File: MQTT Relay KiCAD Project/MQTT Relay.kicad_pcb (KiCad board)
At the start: 2 copper layers, 63.5 x 53.3 mm, 19 parts, among them J1 Power, J2 Temp 0, J3 Input 0, J4 Input 1, J5 Relay 0, J6 Relay 1, SW1 SW_Push, SW2 SW_Push, SW3 SW_Push, U1 SSD1306_128x32

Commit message: Added DFPlayer support
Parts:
- added J7: Line Out, TerminalBlock_Phoenix:TerminalBlock_Phoenix_MPT-0,5-3-2.54_1x03_P2.54mm_Horizontal, F.Cu at (147.3, 78.1)
- added R5: 1K, Resistor_THT:R_Axial_DIN0207_L6.3mm_D2.5mm_P10.16mm_Horizontal, F.Cu at (128.9, 71.8)
- added U2: DFPlayer_Module, Module:Module_DIP16_17.8mm, F.Cu at (139.7, 60.3)
- moved J1 56.8 mm to (77.5, 77.5), turned to -90 degrees
- moved J2 45.4 mm to (147.3, 87.6)
- moved J6 28.5 mm to (148.6, 40.6), turned to 180 degrees
- moved J5 14.9 mm to (138.4, 40.6), turned to 180 degrees
- moved J3 14.2 mm to (135.9, 86.4), turned to 0 degrees
- moved J4 8.13 mm to (128.3, 86.4), turned to 0 degrees
- moved e 7.62 mm to (125.7, 78.7)
- moved REF** 1.27 mm to (127.0, 40.6)
- moved SW2 1.24 mm to (113.0, 39.4)
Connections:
- net /~CFG renamed /~{CFG}
- A1 pad 15: Net-(A1-Pad15) -> unconnected-(A1-Pad15)
- A1 pad 16: Net-(A1-Pad16) -> unconnected-(A1-Pad16)
- A1 pad 20: Net-(A1-Pad20) -> unconnected-(A1-Pad20)
- A1 pad 21: Net-(A1-Pad21) -> unconnected-(A1-Pad21)
- A1 pad 22: Net-(A1-Pad22) -> unconnected-(A1-Pad22)
- A1 pad 23: Net-(A1-Pad23) -> unconnected-(A1-Pad23)
- A1 pad 24: Net-(A1-Pad24) -> unconnected-(A1-Pad24)
- A1 pad 27: Net-(A1-Pad27) -> unconnected-(A1-Pad27)
- A1 pad 28: Net-(A1-Pad28) -> unconnected-(A1-Pad28)
- A1 pad 3: Net-(A1-Pad3) -> unconnected-(A1-Pad3)
- A1 pad 4: Net-(A1-Pad4) -> unconnected-(A1-Pad4)
- A1 pad 5: Net-(A1-Pad5) -> unconnected-(A1-Pad5)
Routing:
- net GND: track 204.0 -> 294.9 mm
- net Net-(A1-Pad8): track 48.3 -> 95.7 mm
- net +3V3: track 126.6 -> 169.0 mm
- net Net-(A1-Pad6): track 102.9 -> 134.3 mm
- net Net-(A1-Pad11): track 35.7 -> 61.0 mm, vias 0 -> 1
- net Net-(A1-Pad30): track 80.9 -> 105.1 mm, vias 0 -> 1
- net Net-(A1-Pad12): track 31.5 -> 46.6 mm
- net Net-(A1-Pad19): track 66.0 -> 80.5 mm
- net Net-(J7-Pad2): track 0.00 -> 12.0 mm
- net Net-(J7-Pad3): track 0.00 -> 8.45 mm
- net Net-(R5-Pad2): track 0.00 -> 7.29 mm
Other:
- board size 63.5 x 53.3 mm -> 77.5 x 53.3 mm
- net class Default removed
- board text added: "Audio"
- board text added: "MQTT Agent 2 Input, 2 output + Audio (c) 2022 Marc D. Spencer"
- board text removed: "MQTT Agent 2 Input, 2 output (c) 2020 Marc D. Spencer"

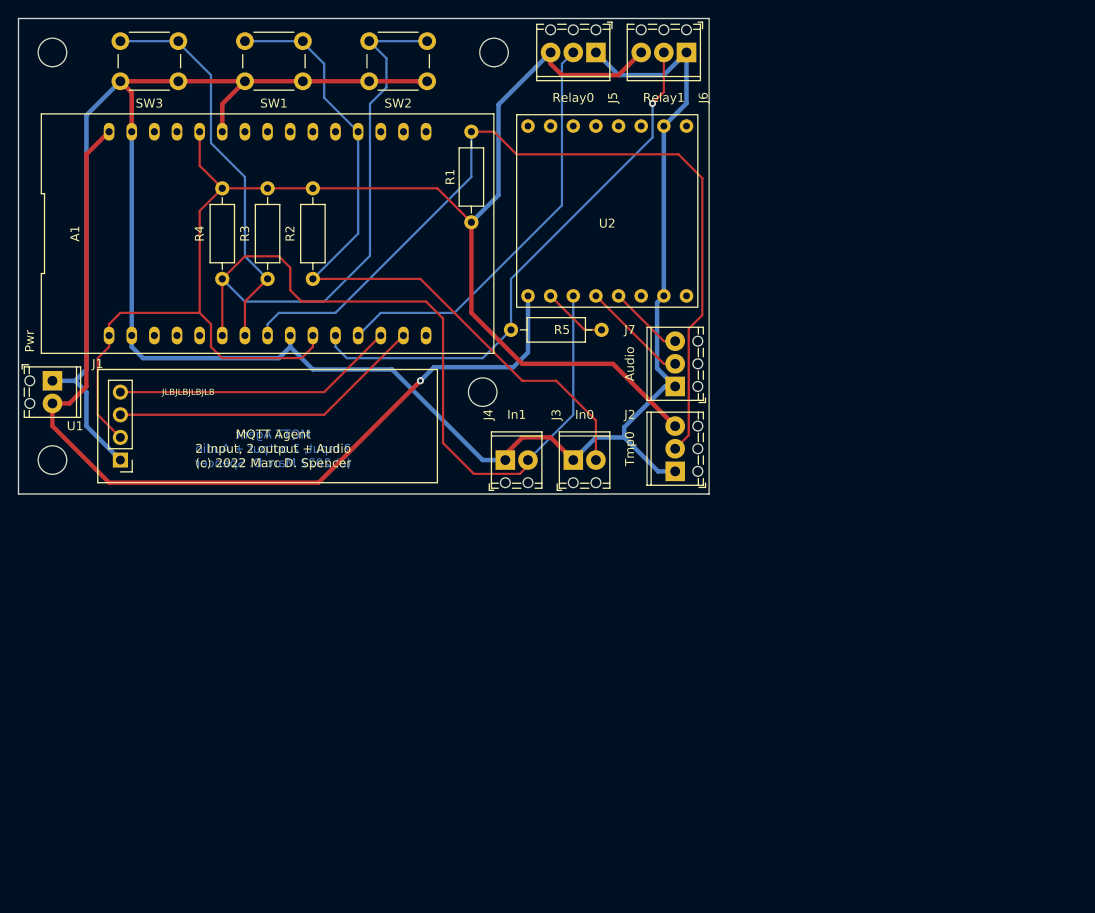
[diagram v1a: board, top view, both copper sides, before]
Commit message: Version 3.0 Board
Integrated relays and SMD
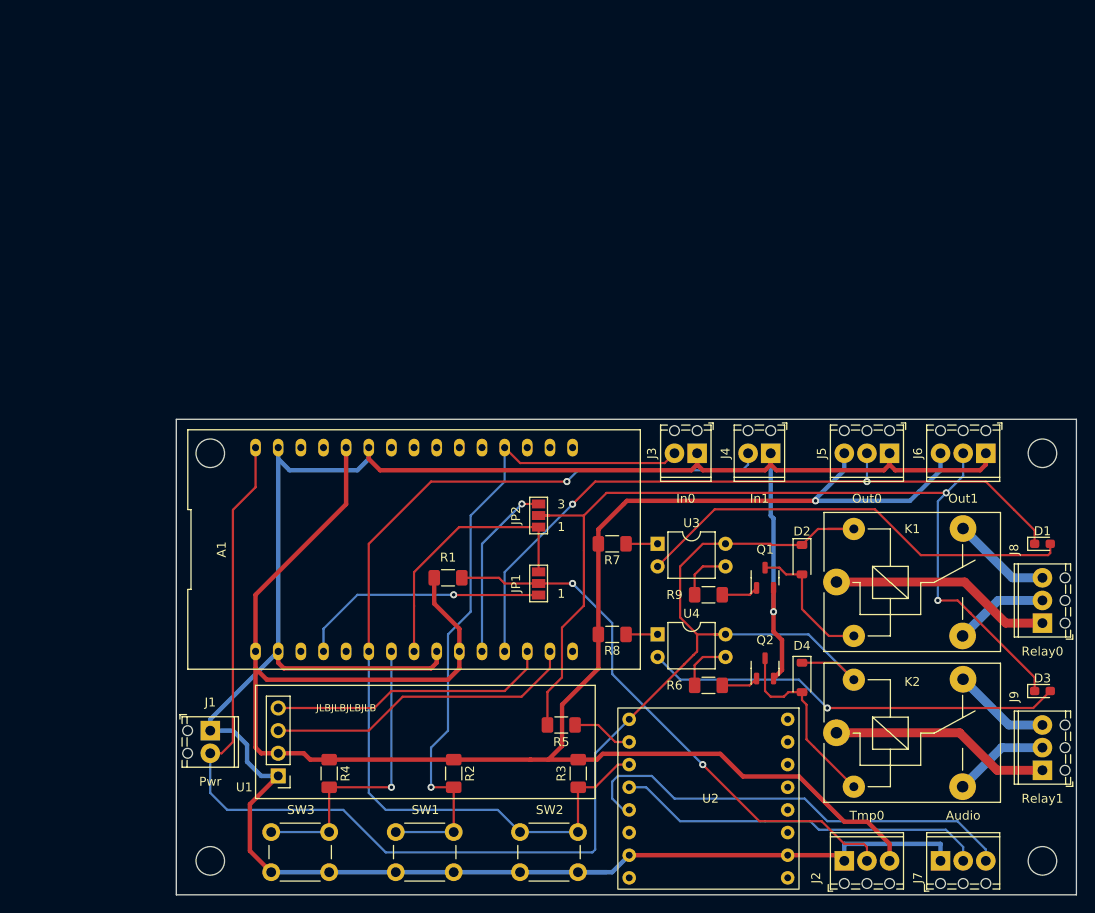
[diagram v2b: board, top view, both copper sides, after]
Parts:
- removed the REF** at (77.5, 86.4)
- removed the REF** at (77.5, 40.6)
- removed the REF** at (127.0, 40.6)
- removed e: MountingHole_3.2mm_M3, MountingHole:MountingHole_3.2mm_M3
- added D1: LED, LED_SMD:LED_0603_1608Metric_Pad1.05x0.95mm_HandSolder, F.Cu at (188.5, 95.8)
- added D2: 1N4148W, Diode_SMD:D_SOD-123, F.Cu at (161.5, 97.5)
- added D3: LED, LED_SMD:LED_0603_1608Metric_Pad1.05x0.95mm_HandSolder, F.Cu at (188.5, 112.3)
- added D4: 1N4148W, Diode_SMD:D_SOD-123, F.Cu at (161.5, 110.7)
- added J8: Relay 0, TerminalBlock_Phoenix:TerminalBlock_Phoenix_MPT-0,5-3-2.54_1x03_P2.54mm_Horizontal, F.Cu at (188.5, 104.6)
- added J9: Relay 1, TerminalBlock_Phoenix:TerminalBlock_Phoenix_MPT-0,5-3-2.54_1x03_P2.54mm_Horizontal, F.Cu at (188.5, 121.2)
- added JP1: T-0, Jumper:SolderJumper-3_P1.3mm_Open_Pad1.0x1.5mm_NumberLabels, F.Cu at (132.0, 100.2)
- added JP2: R-1, Jumper:SolderJumper-3_P1.3mm_Open_Pad1.0x1.5mm_NumberLabels, F.Cu at (132.0, 92.6)
- added K1: G5Q-1, Relay_THT:Relay_SPDT_SANYOU_SRD_Series_Form_C, F.Cu at (165.4, 100.0)
- added K2: G5Q-1, Relay_THT:Relay_SPDT_SANYOU_SRD_Series_Form_C, F.Cu at (165.4, 116.9)
- added Q1: S8050/J3Y, Package_TO_SOT_SMD:SOT-23-3, F.Cu at (157.4, 99.6)
- added Q2: S8050/J3Y, Package_TO_SOT_SMD:SOT-23-3, F.Cu at (157.4, 109.7)
- added R6: 510, Resistor_SMD:R_1206_3216Metric_Pad1.30x1.75mm_HandSolder, F.Cu at (151.1, 111.6)
- added R7: 1K, Resistor_SMD:R_1206_3216Metric_Pad1.30x1.75mm_HandSolder, F.Cu at (140.3, 95.8)
- added R8: 1K, Resistor_SMD:R_1206_3216Metric_Pad1.30x1.75mm_HandSolder, F.Cu at (140.3, 105.9)
- added R9: 510, Resistor_SMD:R_1206_3216Metric_Pad1.30x1.75mm_HandSolder, F.Cu at (151.1, 101.5)
- added REF**: MountingHole_3.2mm_M3, MountingHole:MountingHole_3.2mm_M3, F.Cu at (95.2, 131.3)
- added REF**: MountingHole_3.2mm_M3, MountingHole:MountingHole_3.2mm_M3, F.Cu at (188.5, 85.6)
- added REF**: MountingHole_3.2mm_M3, MountingHole:MountingHole_3.2mm_M3, F.Cu at (188.5, 131.3)
- added REF**: MountingHole_3.2mm_M3, MountingHole:MountingHole_3.2mm_M3, F.Cu at (95.2, 85.6)
- added U3: PC817, Package_DIP:DIP-4_W7.62mm, F.Cu at (145.3, 95.8)
- added U4: PC817, Package_DIP:DIP-4_W7.62mm, F.Cu at (145.3, 105.9)
- J5: value Relay 0 -> Output 0
- J6: value Relay 1 -> Output 1
- R1, R2, R3, R4, R5: footprint Resistor_THT:R_Axial_DIN0207_L6.3mm_D2.5mm_P10.16mm_Horizontal -> Resistor_SMD:R_1206_3216Metric_Pad1.30x1.75mm_HandSolder
- moved SW1 90.3 mm to (116.0, 128.1)
- moved SW2 90.3 mm to (129.9, 128.1)
- moved SW3 90.3 mm to (102.0, 128.1)
- moved R3 76.8 mm to (136.4, 121.5)
- moved R2 67.5 mm to (122.5, 121.5)
- moved R4 66.0 mm to (108.5, 121.5)
- moved U2 64.6 mm to (148.5, 124.3), turned to -90 degrees
- moved J7 61.0 mm to (177.1, 131.3), turned to 0 degrees
- moved J6 56.1 mm to (182.2, 85.6)
- moved J5 55.7 mm to (171.4, 85.6)
- moved J2 47.6 mm to (166.3, 131.3), turned to 0 degrees
- moved R5 44.7 mm to (134.5, 116.1)
- moved J1 43.1 mm to (95.2, 116.7)
- moved R1 40.0 mm to (121.8, 99.6), turned to 0 degrees
- moved U1 39.6 mm to (102.8, 121.8)
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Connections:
- net Net-(A1-Pad30) renamed VCC
- A1 pad 11: Net-(A1-Pad11) -> Net-(A1-D4)
- A1 pad 4: unconnected-(A1-Pad4) -> Net-(A1-RX)
- A1 pad 8: Net-(A1-Pad8) -> Net-(A1-D5)
- J2 pad 2: Net-(A1-Pad8) -> Net-(J2-Pin_2)
- J6 pad 2: Net-(A1-Pad11) -> Net-(D3-K)
- R1 pad 2: Net-(A1-Pad8) -> Net-(J2-Pin_2)
- R5 pad 1: Net-(A1-Pad11) -> Net-(D3-K)
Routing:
- net Net-(D3-K): track 0.00 -> 107.0 mm, vias 0 -> 2
- net Net-(A1-Pad8): track 95.7 -> 0.00 mm
- net VCC: track 105.1 -> 177.4 mm, vias 1 -> 0
- net Net-(J2-Pin_2): track 0.00 -> 62.9 mm, vias 0 -> 2
- net Net-(A1-Pad11): track 61.0 -> 0.00 mm, vias 1 -> 0
- net +3V3: track 169.0 -> 229.7 mm, vias 0 -> 1
- net Net-(D1-A): track 0.00 -> 50.0 mm
- net Net-(D3-A): track 0.00 -> 47.2 mm, vias 0 -> 1
- net Net-(J7-Pin_3): track 8.45 -> 51.2 mm
- net Net-(A1-D3): track 46.6 -> 79.5 mm, vias 0 -> 2
- net Net-(A1-D5): track 0.00 -> 30.0 mm
- net Net-(J7-Pin_2): track 12.0 -> 41.8 mm
- net Net-(A1-RX): track 0.00 -> 28.3 mm, vias 0 -> 1
- net Net-(J8-Pin_1): track 0.00 -> 25.0 mm
- net Net-(J9-Pin_1): track 0.00 -> 24.8 mm
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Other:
- board size 77.5 x 53.3 mm -> 101 x 53.3 mm
- board text added: "MQTT Agent, 3.0 2 Input, 2 Output, 2 Relay + Audio (c) 2023 Marc D. Spencer"
- board text added: "Out0"
- board text added: "Out1"
- board text removed: "MQTT Agent 2 Input, 2 output + Audio (c) 2022 Marc D. Spencer"

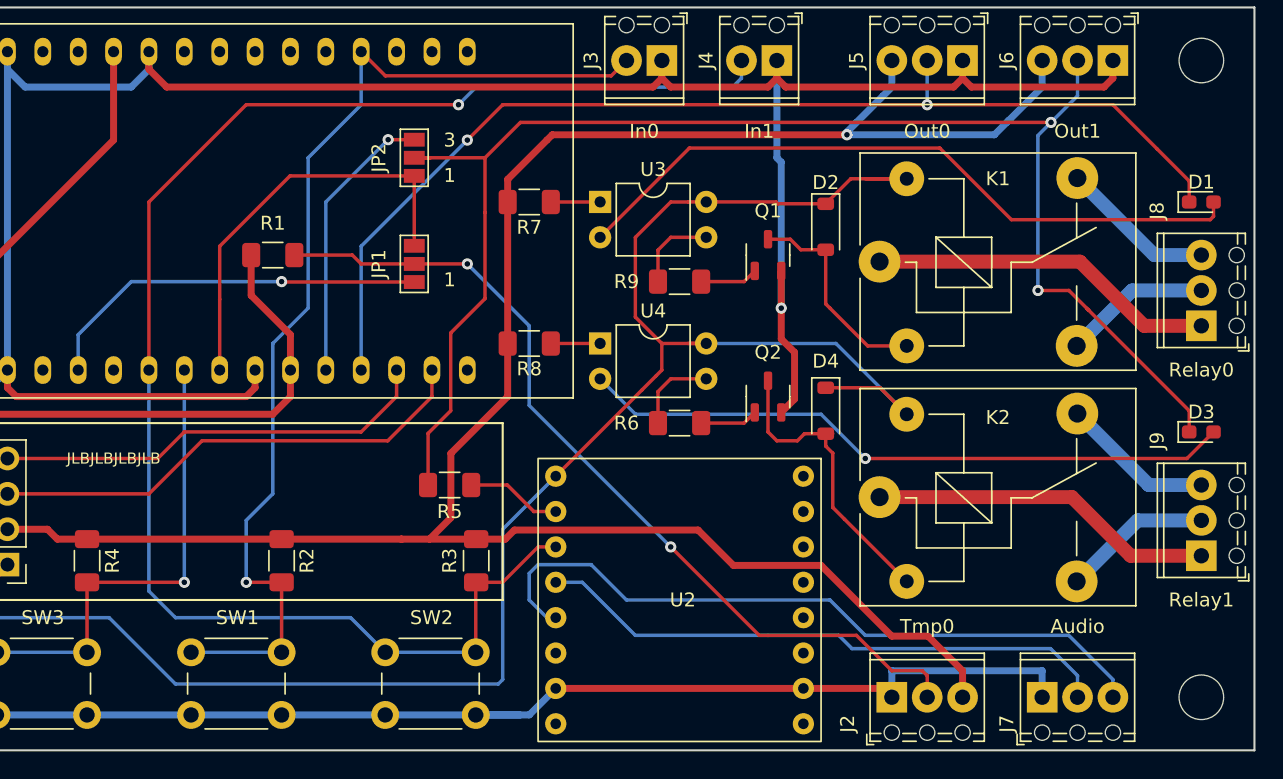
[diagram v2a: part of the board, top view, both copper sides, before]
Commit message: Added Relays onBoard
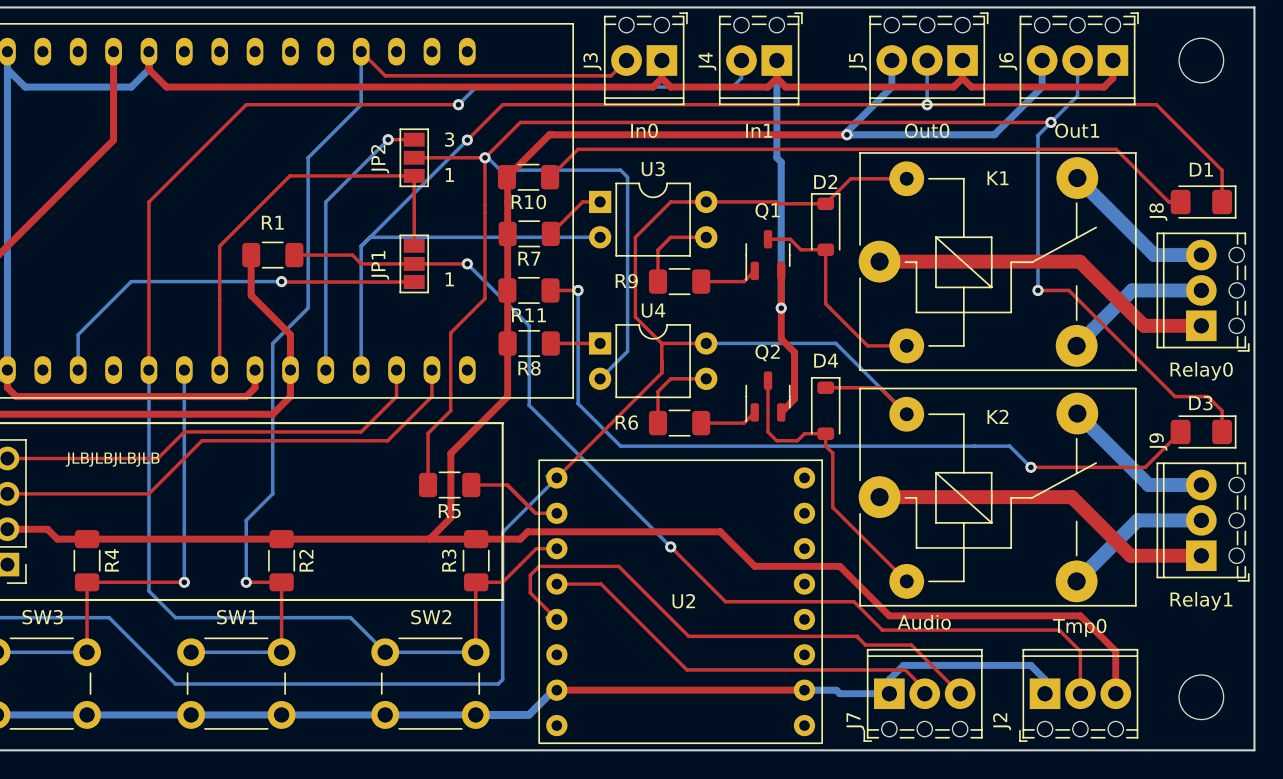
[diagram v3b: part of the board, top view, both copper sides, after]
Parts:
- added R10: 120, Resistor_SMD:R_1206_3216Metric_Pad1.30x1.75mm_HandSolder, F.Cu at (140.2, 94.0)
- added R11: 120, Resistor_SMD:R_1206_3216Metric_Pad1.30x1.75mm_HandSolder, F.Cu at (140.2, 102.1)
- D1, D3: footprint LED_SMD:LED_0603_1608Metric_Pad1.05x0.95mm_HandSolder -> LED_SMD:LED_1206_3216Metric_Pad1.42x1.75mm_HandSolder
- R7, R8: value 1K -> 120
- moved J2 11.0 mm to (177.3, 131.1)
- moved J7 11.0 mm to (166.1, 131.1)
- moved R7 2.29 mm to (140.3, 98.0)
- moved U2 0.15 mm to (148.6, 124.5)
- turned D1 to 180 degrees
- turned D3 to 180 degrees
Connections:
- U3 pad 2: Net-(D1-A) -> Net-(A1-D3)
- U4 pad 2: Net-(D3-A) -> Net-(D3-K)
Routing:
- net Net-(D3-K): track 107.0 -> 134.1 mm, vias 2 -> 3
- net Net-(A1-D3): track 79.5 -> 99.7 mm
- net Net-(J7-Pin_2): track 41.8 -> 29.9 mm
- net Net-(J2-Pin_2): track 62.9 -> 74.6 mm
- net Net-(J7-Pin_3): track 51.2 -> 39.5 mm
- net +3V3: track 229.7 -> 240.4 mm
- net Net-(D3-A): track 47.2 -> 56.7 mm, vias 1 -> 2
- net GND: track 282.1 -> 289.3 mm
- net VCC: track 177.4 -> 173.8 mm
- net Net-(U2-RX): track 6.86 -> 9.68 mm
- net Net-(D1-A): track 50.0 -> 47.7 mm
- net Net-(R7-Pad1): track 3.54 -> 4.50 mm
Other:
- board text added: "MQTT Agent, 4.0 2 Input, 2 Output, 2 Relay + Audio (c) 2023 Marc D. Spencer"
- board text removed: "MQTT Agent, 3.0 2 Input, 2 Output, 2 Relay + Audio (c) 2023 Marc D. Spencer"
